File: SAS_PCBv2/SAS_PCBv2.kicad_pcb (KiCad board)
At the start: 2 copper layers, 150 x 100.5 mm, 37 parts, among them J1 BMP280, J10 Conn_01x04, J11 Conn_01x04, J12 Conn_01x04, J13 Adatateur FTDI (Radio RFD900x), J2 GPIO_CONNECTOR, J3 Conn_01x02_Pin, J4 Conn_01x02, J5 Conn_01x02, J6 Conn_01x02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

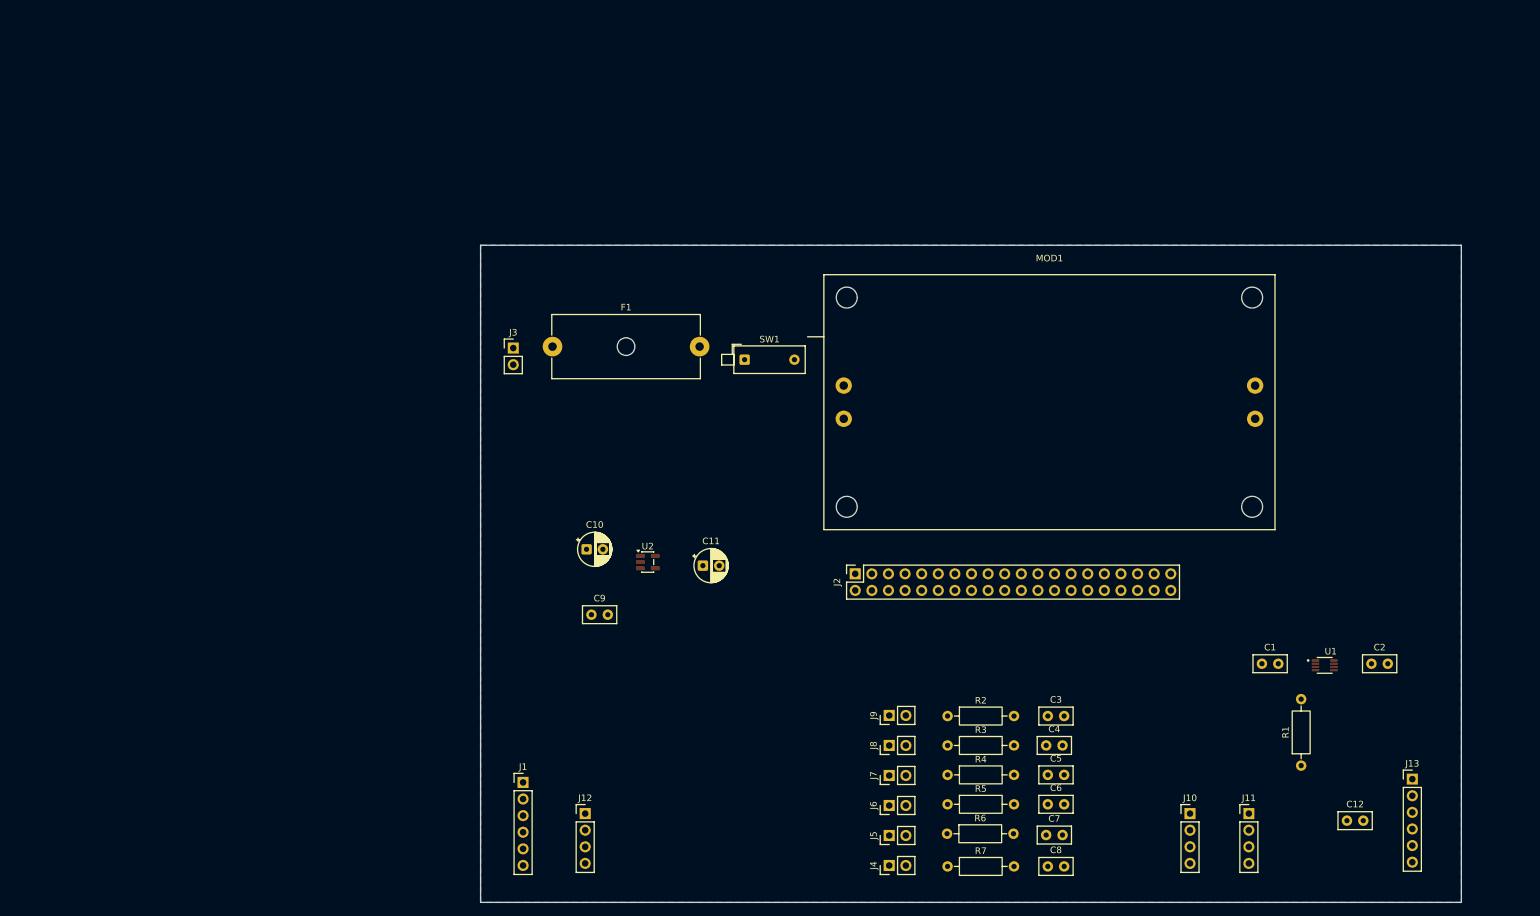
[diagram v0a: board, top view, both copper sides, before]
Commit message: Ajout du connecteur spécial pour les radios, insertion des footprints dans le PCB, fin du schéma
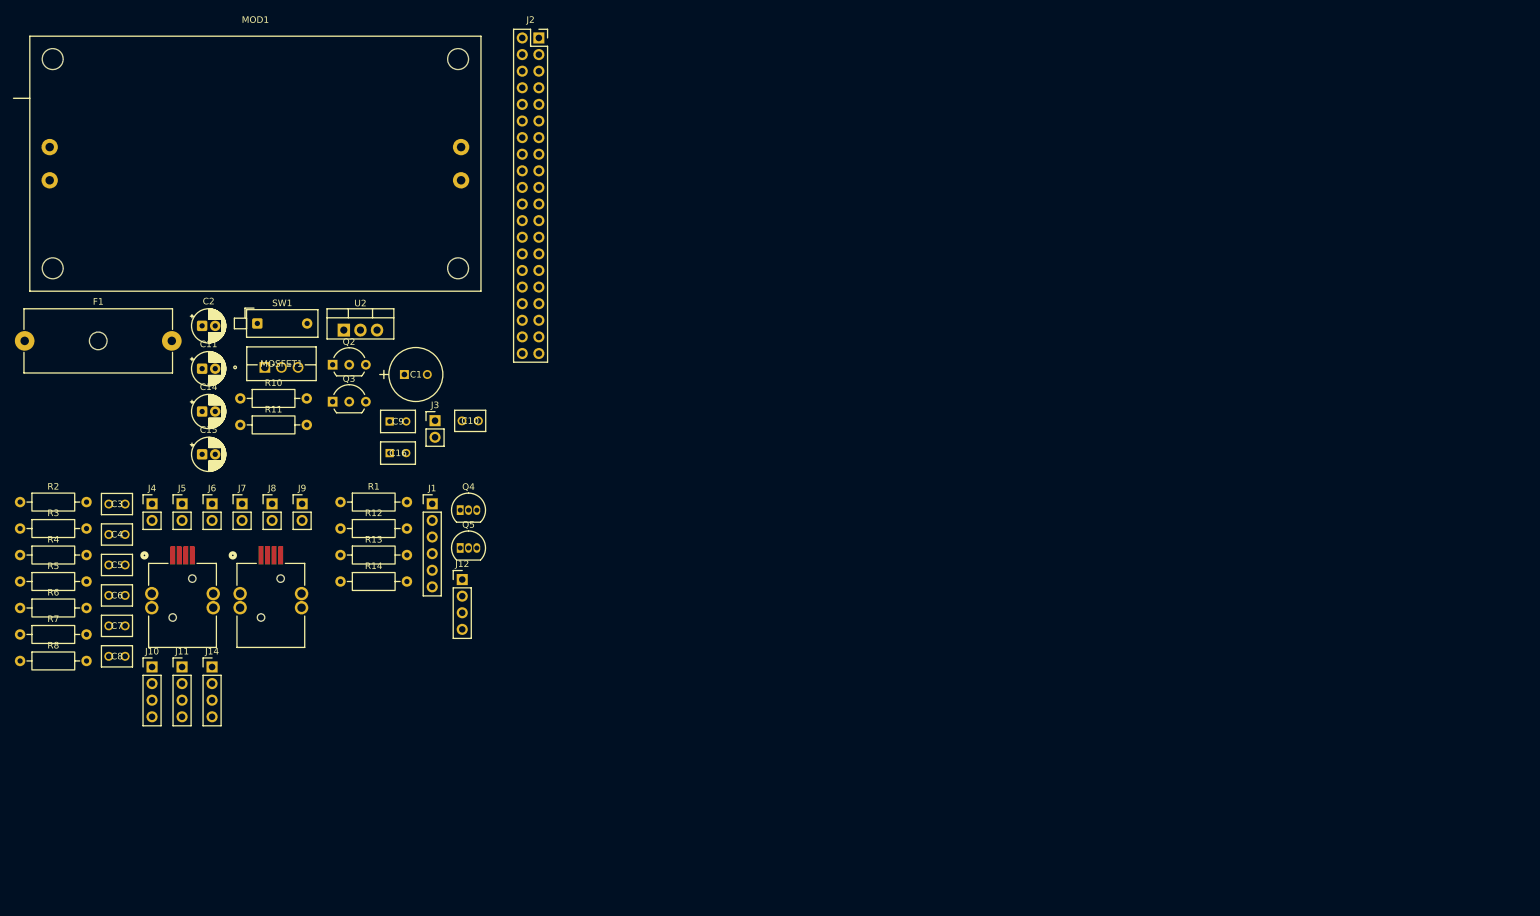
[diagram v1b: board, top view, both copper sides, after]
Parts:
- removed C12: 100nF, Capacitor_THT:C_Disc_D5.0mm_W2.5mm_P2.50mm
- removed J13: Adatateur FTDI (Radio RFD900x), Connector_PinHeader_2.54mm:PinHeader_1x06_P2.54mm_Vertical
- removed U1: TXS0102DCUT, SAS_PCBv2_footprint:SOP50P310X90-8N
- added C14: 1uF, Capacitor_THT:CP_Radial_D5.0mm_P2.00mm, F.Cu at (47.9, 79.4)
- added C15: 1uF, Capacitor_THT:CP_Radial_D5.0mm_P2.00mm, F.Cu at (47.9, 86.0)
- added C16: 0.1uF, SAS_PCBv2_footprint:CAP_C320_KEM, F.Cu at (76.6, 85.8)
- added J14: Fan PWM, Connector_PinHeader_2.54mm:PinHeader_1x04_P2.54mm_Vertical, F.Cu at (49.4, 118.5)
- added J16: GT17HN-4DP-2HD56, SAS_PCBv2_footprint:CONN4_GT17HN_HIR, F.Cu at (45.1, 108.2)
- added J17: GT17HN-4DP-2HD56, SAS_PCBv2_footprint:CONN4_GT17HN_HIR, F.Cu at (58.6, 108.2)
- added MOSFET1: FQPF47P06, SAS_PCBv2_footprint:PMOS_FQP_ONS, F.Cu at (57.5, 72.7)
- added Q2: 2N4403, SAS_PCBv2_footprint:PBIP_2N4403_DIO, F.Cu at (67.9, 72.3)
- added Q3: 2N4403, SAS_PCBv2_footprint:PBIP_2N4403_DIO, F.Cu at (67.9, 77.9)
- added Q4: BS170, Package_TO_SOT_THT:TO-92_Inline, F.Cu at (87.4, 94.5)
- added Q5: BS170, Package_TO_SOT_THT:TO-92_Inline, F.Cu at (87.4, 100.3)
- added R10: 10k, Resistor_THT:R_Axial_DIN0207_L6.3mm_D2.5mm_P10.16mm_Horizontal, F.Cu at (53.8, 77.4)
- added R11: 47k, Resistor_THT:R_Axial_DIN0207_L6.3mm_D2.5mm_P10.16mm_Horizontal, F.Cu at (53.8, 81.5)
- added R12: 10k, Resistor_THT:R_Axial_DIN0207_L6.3mm_D2.5mm_P10.16mm_Horizontal, F.Cu at (69.1, 97.3)
- added R13: 10k, Resistor_THT:R_Axial_DIN0207_L6.3mm_D2.5mm_P10.16mm_Horizontal, F.Cu at (69.1, 101.4)
- added R14: 10k, Resistor_THT:R_Axial_DIN0207_L6.3mm_D2.5mm_P10.16mm_Horizontal, F.Cu at (69.1, 105.4)
- added R8: 10k, Resistor_THT:R_Axial_DIN0207_L6.3mm_D2.5mm_P10.16mm_Horizontal, F.Cu at (20.1, 117.6)
- C1: value 100nF -> 100uF; footprint Capacitor_THT:C_Disc_D5.0mm_W2.5mm_P2.50mm -> SAS_PCBv2_footprint:CAP_RR71_NIC
- C10: value 10uF -> 2.2uF; footprint Capacitor_THT:CP_Radial_D5.0mm_P2.50mm -> SAS_PCBv2_footprint:CAP_FG14_TDK
- C11: footprint Capacitor_THT:CP_Radial_D5.0mm_P2.50mm -> Capacitor_THT:CP_Radial_D5.0mm_P2.00mm
- C2: value 100nF -> 10uF; footprint Capacitor_THT:C_Disc_D5.0mm_W2.5mm_P2.50mm -> Capacitor_THT:CP_Radial_D5.0mm_P2.00mm
- C3, C4, C5, C6, C7, C8: value 100nF -> 2.2uF; footprint Capacitor_THT:C_Disc_D5.0mm_W2.5mm_P2.50mm -> SAS_PCBv2_footprint:CAP_FG14_TDK
- C9: value 10nF -> 0.1uF; footprint Capacitor_THT:C_Disc_D5.0mm_W2.5mm_P2.50mm -> SAS_PCBv2_footprint:CAP_C320_KEM
- J1: value BMP280 -> GY-BMP280
- J12: value Conn_01x04 -> GY-GPS6MV2
- J2: value GPIO_CONNECTOR -> Raspberry Pi 4 Model B
- R2, R3, R4, R5, R6, R7: value 33k -> 10k
- U2: value SPX3819M5-L-3-3 -> LF33_TO220; footprint Package_TO_SOT_SMD:SOT-23-5 -> Package_TO_SOT_THT:TO-220-3_Vertical
- moved C2 186.2 mm to (47.9, 66.3)
- moved J11 164.7 mm to (44.8, 118.5)
- moved J10 160.3 mm to (40.3, 118.5)
- moved R1 152.4 mm to (69.1, 93.3), turned to 0 degrees
- moved C3 147.2 mm to (33.6, 93.6)
- moved C8 147.2 mm to (33.6, 116.9)
- moved C5 147.2 mm to (33.6, 102.9)
- moved C6 147.1 mm to (33.6, 107.6)
- moved C4 146.9 mm to (33.6, 98.2)
- moved C7 146.9 mm to (33.6, 112.2)
- moved R7 146.2 mm to (20.1, 113.5)
- moved R6 145.9 mm to (20.1, 109.5)
- moved R5 145.9 mm to (20.1, 105.4)
- moved R4 145.8 mm to (20.1, 101.4)
- moved R3 145.7 mm to (20.1, 97.3)
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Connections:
- C1 pad 1: GND -> VIN
- C1 pad 2: +5V -> GND
- C10 pad 1: GND -> +3V3
- C10 pad 2: +5V -> GND
- C11 pad 1: GND -> +5V
- C11 pad 2: +3V3 -> GND
- C2 pad 1: GND -> VIN
- C2 pad 2: +3V3 -> GND
- C9 pad 1: Net-(U2-ADJ/BYP) -> +5V
- J1 pad 5: unconnected-(J1-Pin_5-Pad5) -> +3V3
- J2 pad 1: +3V3 -> unconnected-(J2-3V3-Pad1)
- J2 pad 17: +3V3 -> unconnected-(J2-3V3-Pad17)
- J2 pad 2: +5V -> RPI_5V
- J2 pad 21: unconnected-(J2-Pin_21-Pad21) -> UART_RAD2_TX
- J2 pad 24: unconnected-(J2-Pin_24-Pad24) -> UART_RAD2_RX
- J2 pad 29: unconnected-(J2-Pin_29-Pad29) -> UART_RAD1_TX
- J2 pad 32: UART_RADIO_RX -> Vent_PWM
- J2 pad 33: UART_RADIO_TX -> unconnected-(J2-GPIO13-Pad33)
- J2 pad 37: unconnected-(J2-Pin_37-Pad37) -> FAN_TACH
- J2 pad 4: +5V -> RPI_5V
- J2 pad 7: unconnected-(J2-Pin_7-Pad7) -> UART_RAD1_RX
- MOD1 pad 1: +7.5V -> VIN
- R1 pad 2: GND -> I2C_3V3_SCL
- SW1 pad 2: +5V -> VIN
- U2 pad 3: +5V -> +3V3
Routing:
- removed copper zone on B.Cu, net GND
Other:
- board outline removed

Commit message: Composantes placees sur le PCB
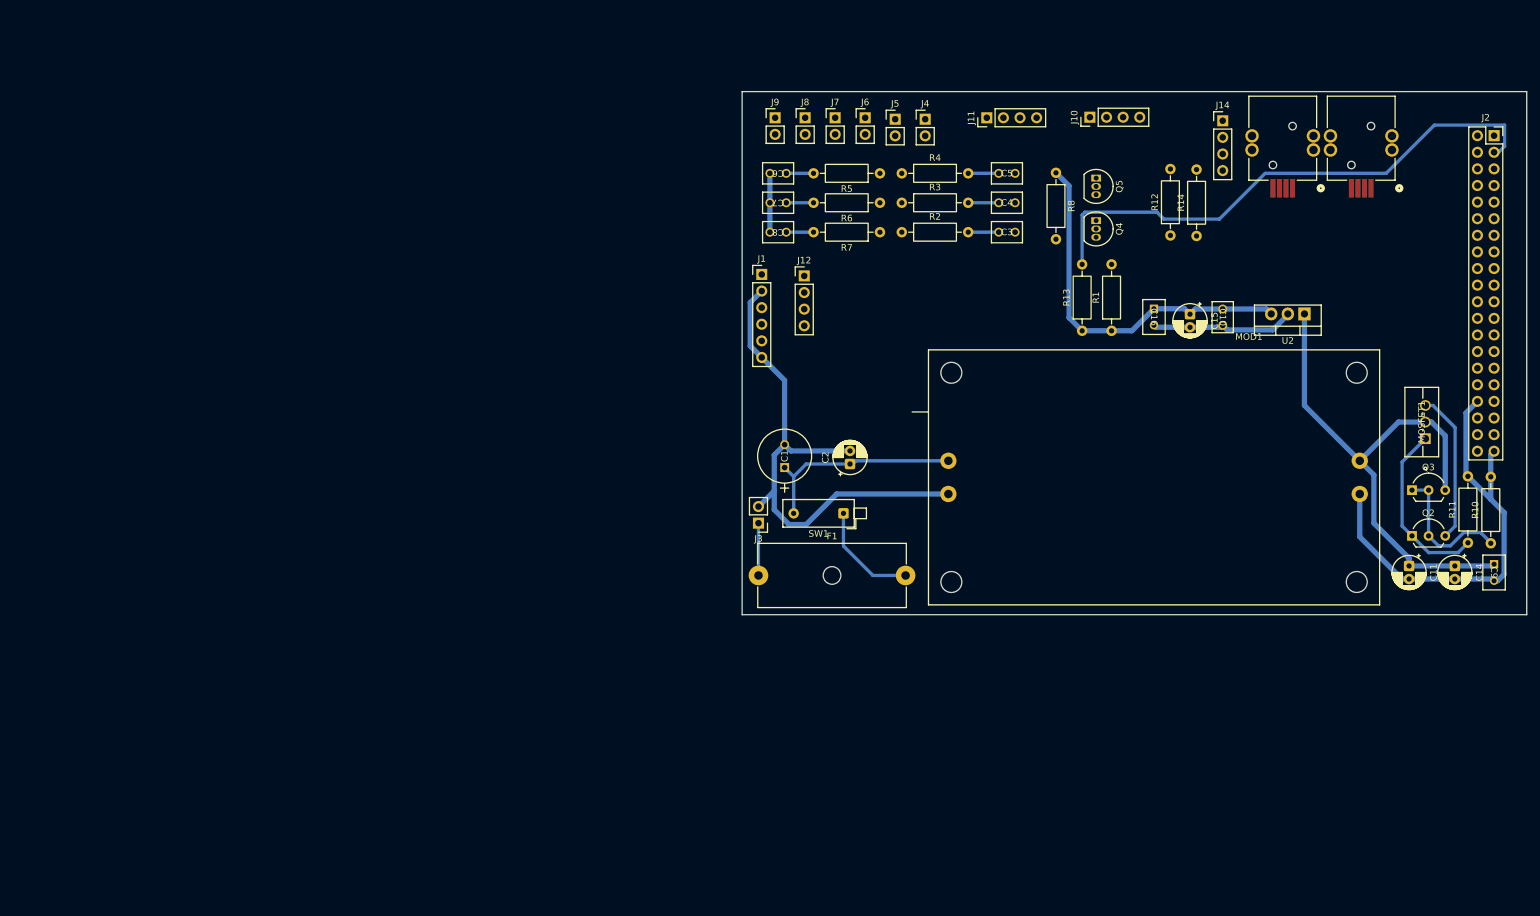
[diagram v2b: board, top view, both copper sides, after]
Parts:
- moved C14 193.0 mm to (239.5, 103.0), turned to -90 degrees
- moved J16 192.9 mm to (225.0, 38.5), turned to 180 degrees
- moved R10 192.5 mm to (245.0, 99.6), turned to 90 degrees
- moved R11 188.6 mm to (241.5, 99.5), turned to 90 degrees
- moved C11 187.0 mm to (232.5, 103.0), turned to -90 degrees
- moved MOSFET1 177.8 mm to (235.0, 83.6), turned to 90 degrees
- moved J14 175.7 mm to (204.0, 35.0)
- moved R8 175.1 mm to (178.5, 42.9), turned to -90 degrees
- moved C9 170.3 mm to (245.5, 102.8), turned to -90 degrees
- moved J17 169.4 mm to (213.0, 38.5), turned to 180 degrees
- moved Q2 167.1 mm to (232.9, 98.5)
- moved J10 166.3 mm to (183.7, 34.4), turned to 90 degrees
- moved Q3 165.6 mm to (232.9, 91.5)
- moved C15 152.6 mm to (199.0, 64.5), turned to -90 degrees
- moved J11 149.0 mm to (167.9, 34.5), turned to 90 degrees
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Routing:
- net GND: track 0.00 -> 180.4 mm
- net I2C_3V3_SDA: track 0.00 -> 83.9 mm
- net +5V: track 0.00 -> 83.0 mm
- net +3V3: track 0.00 -> 57.1 mm
- net VIN: track 0.00 -> 32.2 mm
- net Net-(MOSFET1-G): track 0.00 -> 27.2 mm
- net RPI_5V: track 0.00 -> 23.2 mm
- net Net-(Q2-B): track 0.00 -> 21.3 mm
- net Net-(SW1-A): track 0.00 -> 16.4 mm
- net Net-(J3-Pin_1): track 0.00 -> 8.00 mm
- net BTN_3: track 0.00 -> 4.67 mm
- net BTN_2: track 0.00 -> 4.67 mm
- net BTN_1: track 0.00 -> 4.67 mm
- net BTN_6: track 0.00 -> 4.22 mm
- net BTN_5: track 0.00 -> 4.17 mm
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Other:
- board outline added: 120 x 80 mm

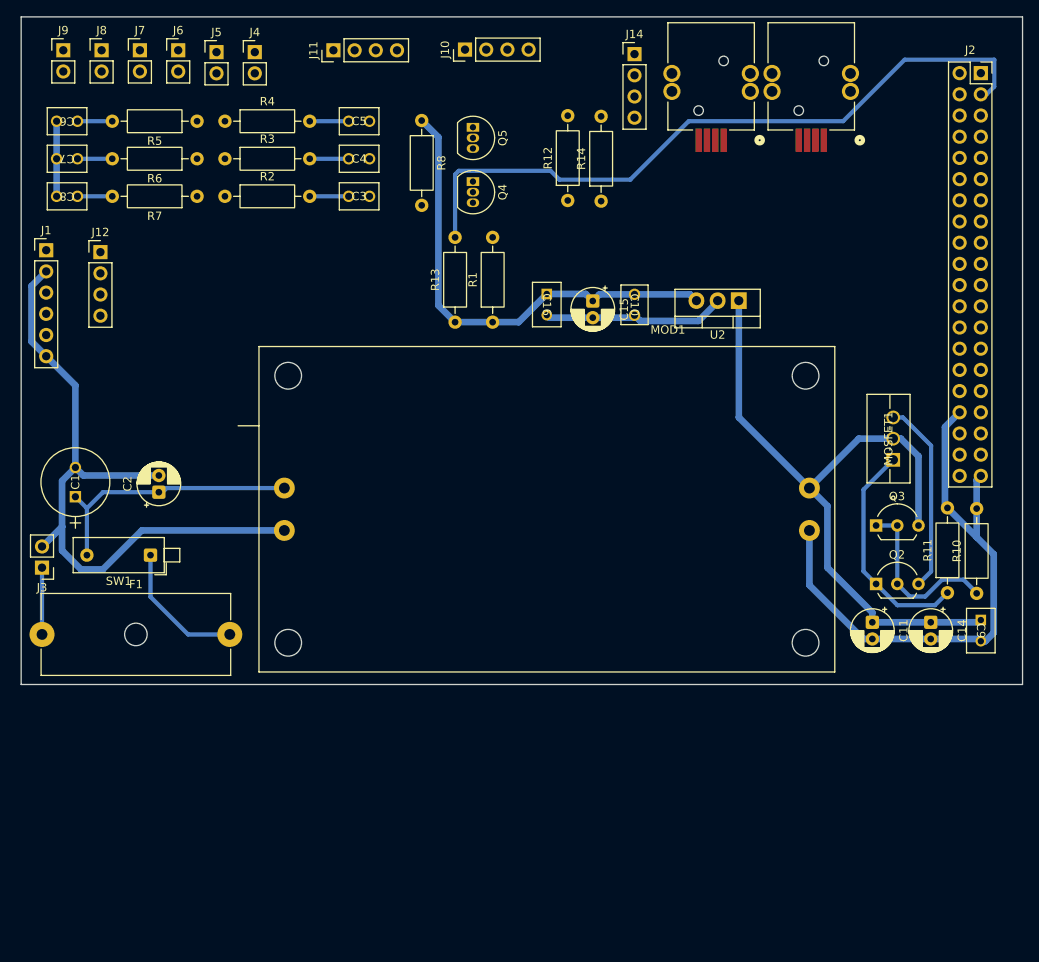
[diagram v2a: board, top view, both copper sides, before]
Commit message: PCB prêt à être routé
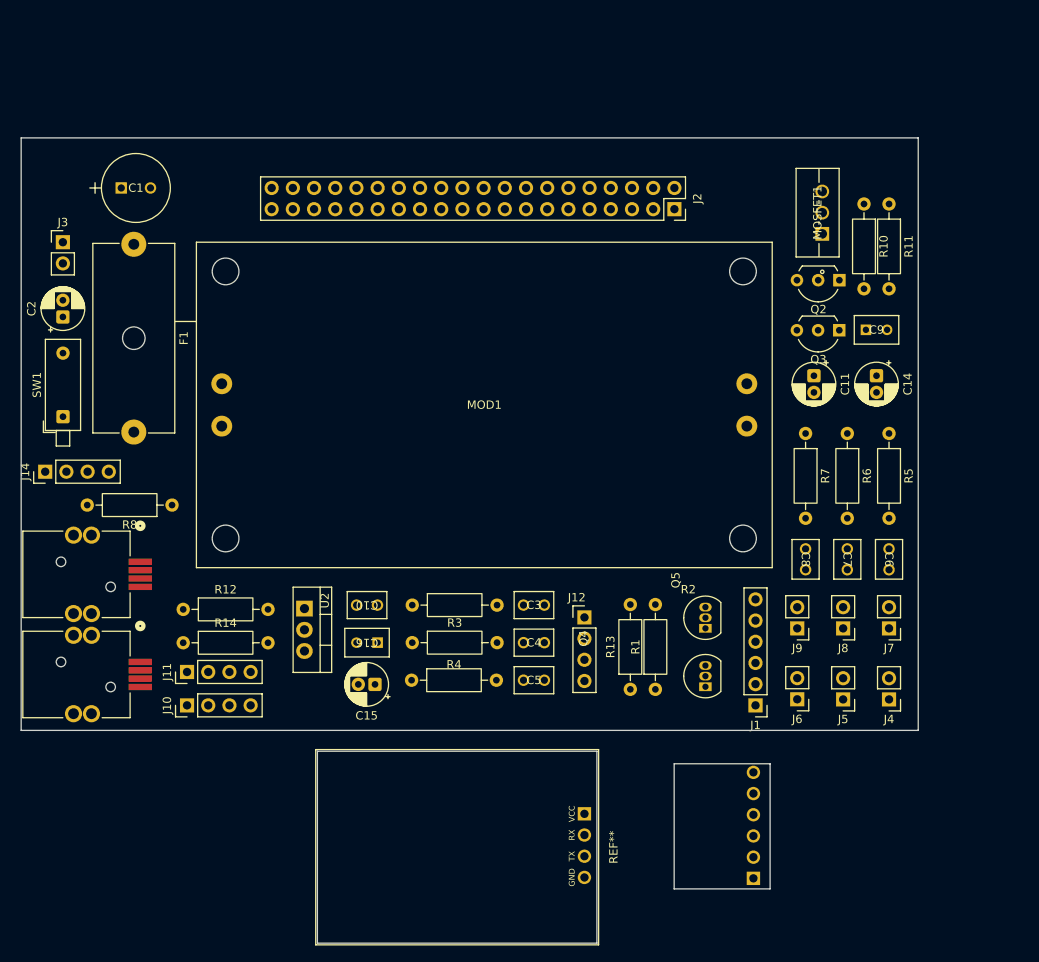
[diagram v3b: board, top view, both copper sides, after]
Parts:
- added REF**: GY-GPS6MV2, SAS_PCBv2_footprint:GY-GPS6MV2_Module, F.Cu at (199.5, 118.5)
- added REF**: GY-BMP280, SAS_PCBv2_footprint:GY-BMP280_Module, B.Cu at (208.8, 135.0)
- moved J7 113.4 mm to (234.5, 103.8), turned to 180 degrees
- moved J8 112.7 mm to (229.0, 103.8), turned to 180 degrees
- moved J9 112.0 mm to (223.5, 103.8), turned to 180 degrees
- moved C6 109.9 mm to (234.5, 94.2), turned to -90 degrees
- moved J4 108.6 mm to (234.5, 112.3), turned to 180 degrees
- moved J5 108.0 mm to (229.0, 112.3), turned to 180 degrees
- moved J6 107.5 mm to (223.5, 112.3), turned to 180 degrees
- moved J16 105.1 mm to (138.0, 97.5), turned to -90 degrees
- moved C7 103.4 mm to (229.5, 94.2), turned to -90 degrees
- moved J17 103.3 mm to (138.0, 109.5), turned to -90 degrees
- moved J1 101.0 mm to (218.5, 113.0), turned to 180 degrees
- moved C8 96.9 mm to (224.5, 94.2), turned to -90 degrees
- moved R5 91.0 mm to (234.5, 80.4), turned to -90 degrees
- moved J14 86.6 mm to (133.4, 85.0), turned to 90 degrees
- moved J10 85.3 mm to (150.4, 113.0)
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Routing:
- net GND: track 180.4 -> 0.00 mm
- net I2C_3V3_SDA: track 83.9 -> 0.00 mm
- net +5V: track 83.0 -> 0.00 mm
- net +3V3: track 57.1 -> 0.00 mm
- net VIN: track 32.2 -> 0.00 mm
- net Net-(MOSFET1-G): track 27.2 -> 0.00 mm
- net RPI_5V: track 23.2 -> 0.00 mm
- net Net-(Q2-B): track 21.3 -> 0.00 mm
- net Net-(SW1-A): track 16.4 -> 0.00 mm
- net Net-(J3-Pin_1): track 8.00 -> 0.00 mm
- net BTN_3: track 4.67 -> 0.00 mm
- net BTN_2: track 4.67 -> 0.00 mm
- net BTN_1: track 4.67 -> 0.00 mm
- net BTN_6: track 4.22 -> 0.00 mm
- net BTN_5: track 4.17 -> 0.00 mm
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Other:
- board size 120 x 80 mm -> 107.5 x 71 mm
